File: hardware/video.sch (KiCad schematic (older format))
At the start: 28 parts, among them U3 74HCT4053, U4 74HCT86, U5 74HCT4053, U6 LM1881, U7 THS7375

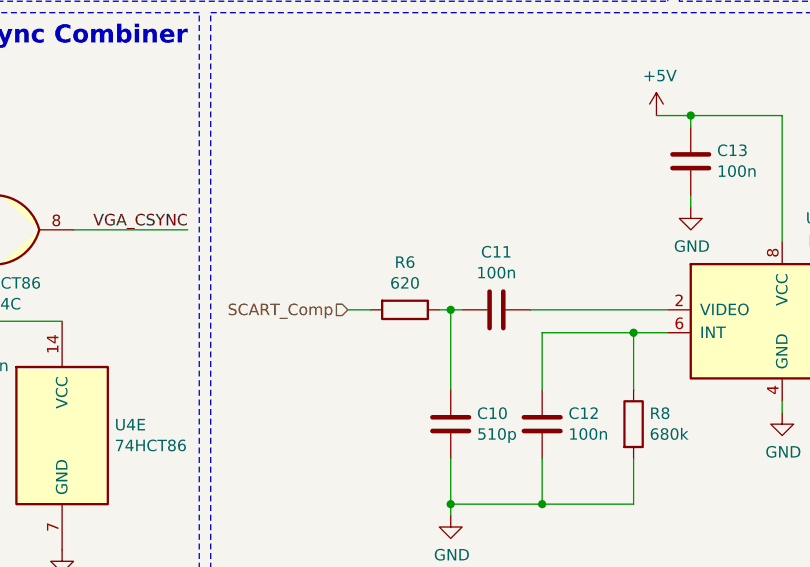
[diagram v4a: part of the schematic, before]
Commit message: Started major rework on the Audio section (chose the wrong amplifier as it can't drive 4Ohm loads) Moved over to nightly Kicad v 5.9 versions. Was a mistake to do, but will look into reverting another time.
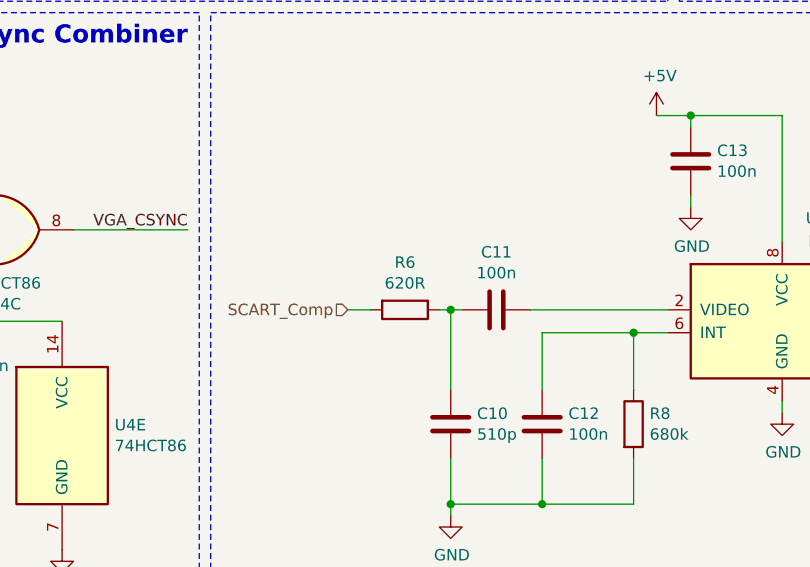
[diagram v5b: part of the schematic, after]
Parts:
- R6: value 620 -> 620R
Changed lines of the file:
@@
 Sheet 2 4
 Title "JAMMA2Console"
-Date "2020-04-20"
-Rev "1"
+Date "2020-05-01"
+Rev "2"
 Comp "Gold"
 Comment1 ""
@@
 P 5650 4650
 F 0 "R6" V 5443 4650 50  0000 C CNN
-F 1 "620" V 5534 4650 50  0000 C CNN
+F 1 "620R" V 5534 4650 50  0000 C CNN
 F 2 "Resistor_SMD:R_0603_1608Metric" V 5580 4650 50  0001 C CNN
 F 3 "~" H 5650 4650 50  0001 C CNN
